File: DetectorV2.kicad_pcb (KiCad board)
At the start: 2 copper layers, 20 parts, among them J1 Conn_01x02

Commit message: updated
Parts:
- added TP1: -, Connector_PinHeader_1.00mm:PinHeader_1x01_P1.00mm_Vertical, F.Cu at (77.5, 52.0)
- added TP2: +, Connector_PinHeader_1.00mm:PinHeader_1x01_P1.00mm_Vertical, F.Cu at (83.0, 52.0)
- added U1: AD8092ARZ-REEL7, footprints:R_8_ADI, F.Cu at (84.5, 77.0)
- moved C7 40.6 mm to (83.5, 57.0)
- moved J1 25.5 mm to (124.5, 80.5)
- moved C2 23.6 mm to (79.5, 84.0)
- moved R8 23.4 mm to (108.0, 83.5), turned to 180 degrees
- moved R3 19.8 mm to (75.4, 67.0)
- moved C1 18.6 mm to (75.5, 72.5)
- moved R5 18.3 mm to (101.9, 68.0)
- moved D1 17.3 mm to (44.1, 71.4)
- moved D2 17.3 mm to (44.1, 77.5)
- moved D3 17.3 mm to (33.6, 71.4)
- moved D4 17.3 mm to (33.6, 77.5)
- moved C5 16.9 mm to (95.0, 84.5), turned to 180 degrees
- moved C6 16.8 mm to (105.0, 78.5)
- moved C3 12.2 mm to (90.0, 71.0)
- moved R7 11.6 mm to (90.0, 86.5), turned to -90 degrees
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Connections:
- C7 pad 1: GND -> VCC

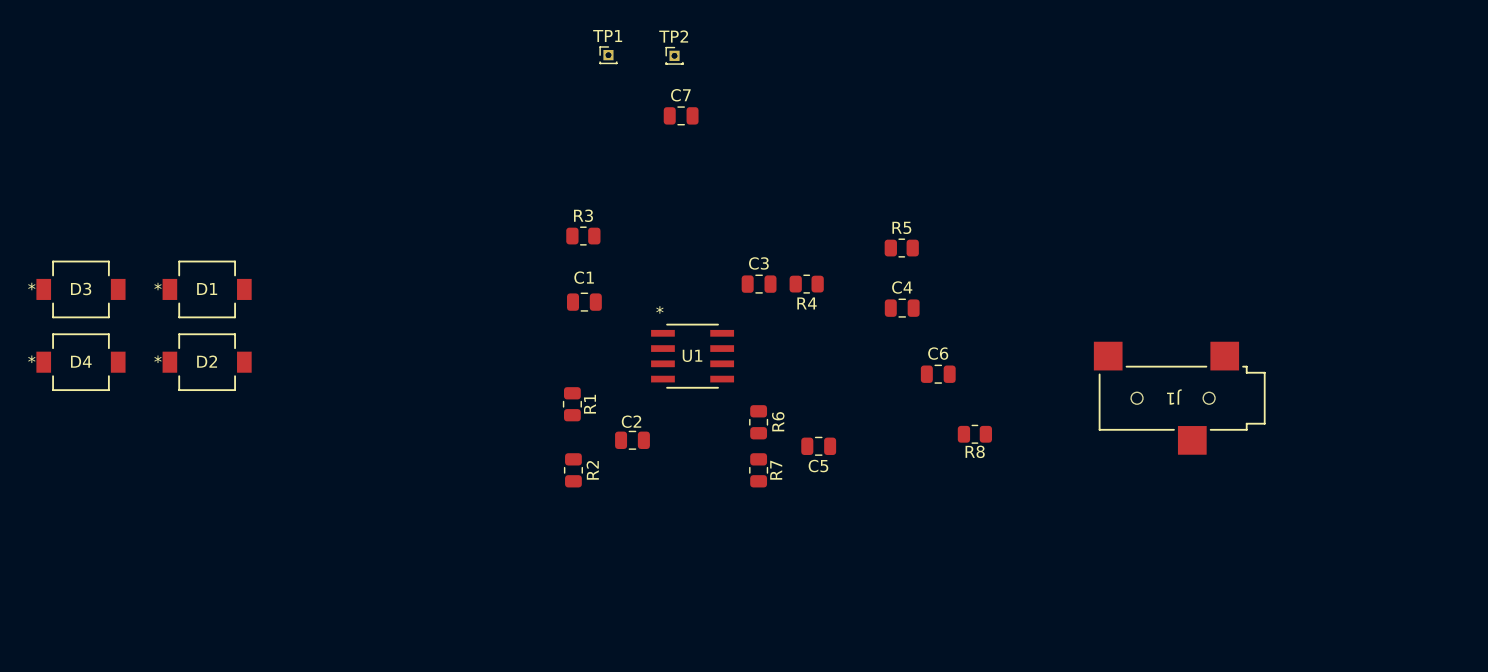
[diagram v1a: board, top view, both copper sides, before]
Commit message: updated version - mit schalter + 47uF footprint
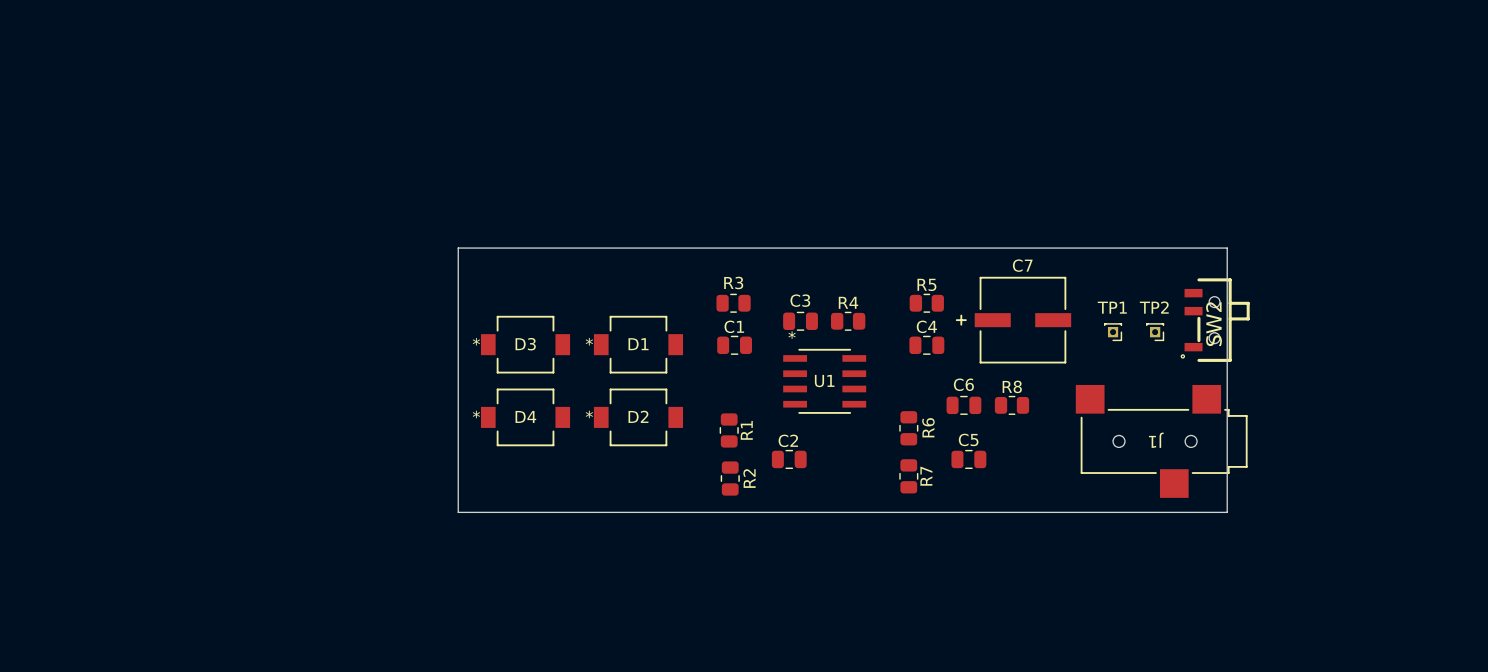
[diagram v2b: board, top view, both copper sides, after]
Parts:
- added SW2: SW_SPST, footprints:SSSS810701, F.Cu at (126.2, 73.2)
- C7: footprint Capacitor_SMD:C_0805_2012Metric -> footprints:PCAP_EEHZ_D_PAN
- moved TP1 47.9 mm to (119.5, 75.0), turned to 180 degrees
- moved TP2 46.1 mm to (123.0, 75.0), turned to 180 degrees
- moved D3 37.3 mm to (70.6, 76.0)
- moved D4 37.3 mm to (70.6, 82.1)
- moved D1 36.2 mm to (80.0, 76.0)
- moved D2 36.2 mm to (80.0, 82.1)
- moved C7 33.1 mm to (112.0, 74.0)
- moved R3 13.7 mm to (87.9, 72.6)
- moved R1 13.2 mm to (87.5, 83.2)
- moved C2 13.1 mm to (92.5, 85.6)
- moved R2 13.1 mm to (87.6, 87.2)
- moved C1 13.0 mm to (88.0, 76.1)
- moved C5 12.5 mm to (107.5, 85.6)
- moved R6 12.5 mm to (102.5, 83.0)
- moved R7 12.5 mm to (102.5, 87.0)
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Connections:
- TP2 pad 1: VCC -> Net-(SW2-A)
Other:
- board outline added: 64 x 22 mm

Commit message: updated mit allen teilen aber fehlerhaft
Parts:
- added C2: 10p, Capacitor_SMD:C_0805_2012Metric, F.Cu at (89.0, 78.0)
- C1: value 5p -> 10p
- moved D2 6.23 mm to (79.0, 75.9), turned to 180 degrees
- moved TP1 6.13 mm to (123.5, 79.7)
- moved D1 6.04 mm to (79.0, 82.0), turned to 180 degrees
- moved C5 3.10 mm to (104.0, 73.0), turned to 0 degrees
- moved R8 2.91 mm to (111.0, 84.0)
- moved R5 2.59 mm to (104.0, 70.0), turned to 0 degrees
- moved C4 1.55 mm to (95.0, 74.0)
- moved R4 1.55 mm to (99.0, 74.0), turned to 0 degrees
- moved C6 1.55 mm to (106.0, 85.6)
- moved R6 1.55 mm to (101.0, 83.0)
- moved R7 1.55 mm to (101.0, 87.0)
- moved C1 1.38 mm to (89.0, 75.1)
- moved R3 1.24 mm to (89.0, 72.0)
- moved TP2 1.20 mm to (123.0, 76.2)
- moved C8 1.00 mm to (113.0, 74.0)
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- renumbered C2 to C3, C3 to C4, C4 to C5, C5 to C6, C6 to C7, C7 to C8
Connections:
- C1 pad 2: Net-(U1-OUT1) -> Net-(C1-Pad2)
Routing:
- net GND: track 0.00 -> 128.5 mm, vias 0 -> 4
- net /input_signal: track 0.00 -> 89.3 mm
- net VCC: track 0.00 -> 38.7 mm, vias 0 -> 4
- net Net-(U1-OUT2): track 0.00 -> 28.6 mm
- net /output_signal: track 0.00 -> 24.8 mm
- net Net-(U1--IN2): track 0.00 -> 17.5 mm
- net Net-(U1-+IN2): track 0.00 -> 15.9 mm
- net Net-(U1-+IN1): track 0.00 -> 15.4 mm
- net Net-(U1-OUT1): track 0.00 -> 13.2 mm
- net Net-(C1-Pad2): track 0.00 -> 3.67 mm
- net Net-(SW2-A): track 0.00 -> 3.22 mm
- net Net-(C4-Pad2): track 0.00 -> 2.10 mm
- added copper zone on B.Cu, net GND
- added copper zone on B.Cu, net VCC
- added copper zone on F.Cu, net VCC
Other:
- board size 64 x 22 mm -> 66.3 x 23.1 mm
